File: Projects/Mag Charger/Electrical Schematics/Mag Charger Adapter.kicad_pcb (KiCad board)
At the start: 2 copper layers, 26 x 12.2 mm, 4 parts, among them J1 Conn_01x08, J2 DX07S016JA3R1500

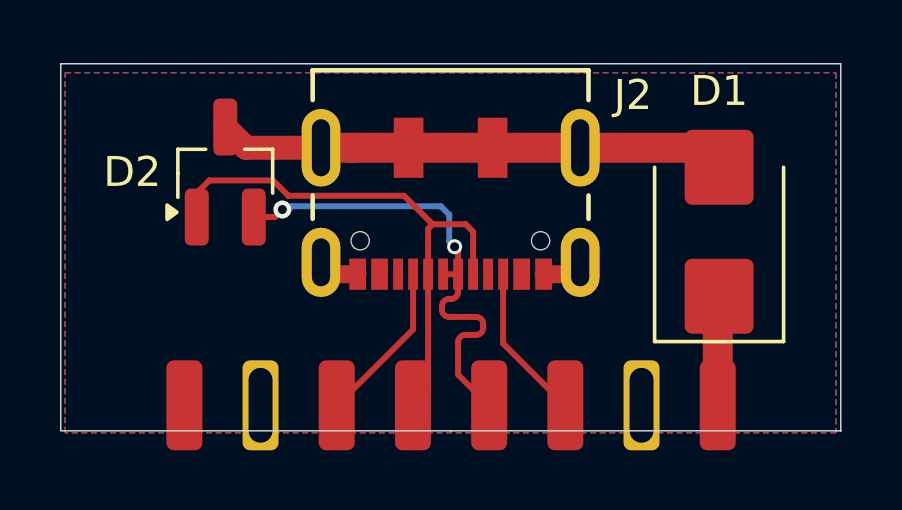
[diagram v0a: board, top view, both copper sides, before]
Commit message: Fixed for manufacturing
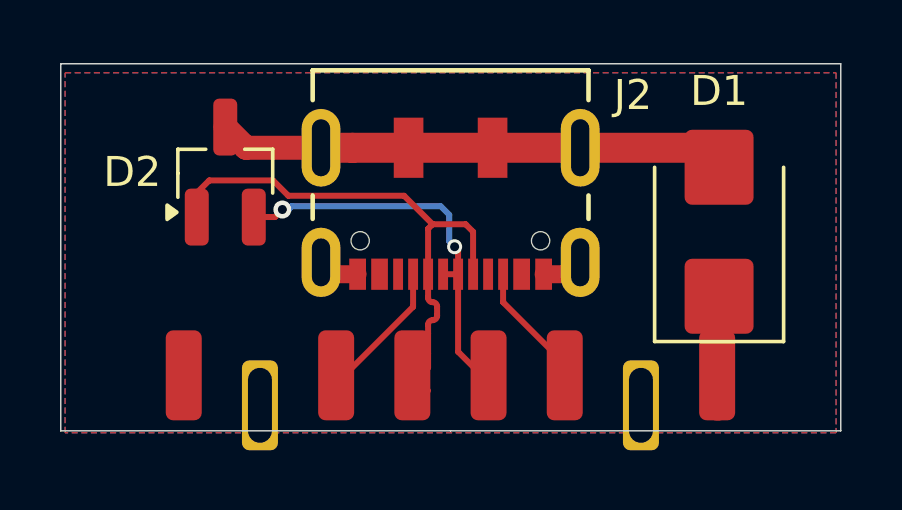
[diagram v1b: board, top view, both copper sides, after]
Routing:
- net /USB_DP: track 16.3 -> 13.4 mm
